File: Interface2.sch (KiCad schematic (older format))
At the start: 6 parts, among them U55 SN74LV165APWR, U56 SN74LV165APWR, U57 SN74LVC126APWR, U58 SN74LVC126APWR

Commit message: PVT
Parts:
- U52: renamed from U55; footprint IC-SOP:TSSOP16-W4.4_Hand -> IC-SOP:TSSOP16-W4.4
- U53: renamed from U56; footprint IC-SOP:TSSOP16-W4.4_Hand -> IC-SOP:TSSOP16-W4.4
- U54: renamed from U57; footprint IC-SOP:TSSOP14-W4.4_Hand -> IC-SOP:TSSOP14-W4.4
- U55: renamed from U58; footprint IC-SOP:TSSOP14-W4.4_Hand -> IC-SOP:TSSOP14-W4.4
- renumbered C238 to C229, C239 to C230
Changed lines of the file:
@@
 $Descr A4 11693 8268
 encoding utf-8
-Sheet 24 24
-Title "Phoenix DVT"
-Date "2020-05-18"
+Sheet 23 24
+Title "Phoenix PVT"
+Date "2020-07-19"
 Rev "1"
 Comp ""
@@
 $EndDescr
 $Comp
-L logic:74165 U56
+L logic:74165 U53
 U 1 1 5E4719EB
 P 2500 4600
-F 0 "U56" H 2500 5350 50  0000 C CNN
+F 0 "U53" H 2500 5350 50  0000 C CNN
 F 1 "SN74LV165APWR" H 2500 3850 50  0000 C CNN
-F 2 "IC-SOP:TSSOP16-W4.4_Hand" H 2500 4600 50  0001 C CNN
+F 2 "IC-SOP:TSSOP16-W4.4" H 2500 4600 50  0001 C CNN
 F 3 "" H 2500 4600 50  0001 C CNN
 F 4 "SN74LV165APWR" H 2500 4600 50  0001 C CNN "PartName"
@@
 P 2000 4400
 AR Path="/5E47EDCF" Ref="#PWR?"  Part="1"
-AR Path="/5F235278/5E47EDCF" Ref="#PWR0446"  Part="1"
-F 0 "#PWR0446" H 2000 4150 50  0001 C CNN
+AR Path="/5F235278/5E47EDCF" Ref="#PWR0426"  Part="1"
+F 0 "#PWR0426" H 2000 4150 50  0001 C CNN
 F 1 "GND" H 2000 4250 50  0000 C CNN
 F 2 "" H 2000 4400 50  0001 C CNN
@@
 P 2000 5200
 AR Path="/5E47F172" Ref="#PWR?"  Part="1"
-AR Path="/5F235278/5E47F172" Ref="#PWR0447"  Part="1"
-F 0 "#PWR0447" H 2000 4950 50  0001 C CNN
+AR Path="/5F235278/5E47F172" Ref="#PWR0427"  Part="1"
+F 0 "#PWR0427" H 2000 4950 50  0001 C CNN
 F 1 "GND" H 2000 5050 50  0000 C CNN
 F 2 "" H 2000 5200 50  0001 C CNN
@@
 	2000 4400 2100 4400
 $Comp
-L supply-value:+3V3 #PWR0445
+L supply-value:+3V3 #PWR0425
 U 1 1 5E48BD16
 P 2000 4000
-F 0 "#PWR0445" H 2000 3850 50  0001 C CNN
+F 0 "#PWR0425" H 2000 3850 50  0001 C CNN
 F 1 "+3V3" H 2000 4140 50  0000 C CNN
 F 2 "" H 2000 4000 50  0001 C CNN
@@
 	2900 5100 3300 5100
 $Comp
-L logic:74165 U55
+L logic:74165 U52
 U 1 1 5E6F7AF5
 P 2500 1600
-F 0 "U55" H 2500 2350 50  0000 C CNN
+F 0 "U52" H 2500 2350 50  0000 C CNN
 F 1 "SN74LV165APWR" H 2500 850 50  0000 C CNN
-F 2 "IC-SOP:TSSOP16-W4.4_Hand" H 2500 1600 50  0001 C CNN
+F 2 "IC-SOP:TSSOP16-W4.4" H 2500 1600 50  0001 C CNN
 F 3 "" H 2500 1600 50  0001 C CNN
 F 4 "SN74LV165APWR" H 2500 1600 50  0001 C CNN "PartName"
@@
 P 2000 1400
 AR Path="/5E6F7AFF" Ref="#PWR?"  Part="1"
-AR Path="/5F235278/5E6F7AFF" Ref="#PWR0443"  Part="1"
-F 0 "#PWR0443" H 2000 1150 50  0001 C CNN
+AR Path="/5F235278/5E6F7AFF" Ref="#PWR0423"  Part="1"
+F 0 "#PWR0423" H 2000 1150 50  0001 C CNN
 F 1 "GND" H 2000 1250 50  0000 C CNN
 F 2 "" H 2000 1400 50  0001 C CNN
@@
 P 2000 2200
 AR Path="/5E6F7B05" Ref="#PWR?"  Part="1"
-AR Path="/5F235278/5E6F7B05" Ref="#PWR0444"  Part="1"
-F 0 "#PWR0444" H 2000 1950 50  0001 C CNN
+AR Path="/5F235278/5E6F7B05" Ref="#PWR0424"  Part="1"
+F 0 "#PWR0424" H 2000 1950 50  0001 C CNN
 F 1 "GND" H 2000 2050 50  0000 C CNN
 F 2 "" H 2000 2200 50  0001 C CNN
@@
 	2000 1400 2100 1400
 $Comp
-L supply-value:+3V3 #PWR0442
+L supply-value:+3V3 #PWR0422
 U 1 1 5E6F7B0D
 P 2000 1000
-F 0 "#PWR0442" H 2000 850 50  0001 C CNN
+F 0 "#PWR0422" H 2000 850 50  0001 C CNN
 F 1 "+3V3" H 2000 1140 50  0000 C CNN
 F 2 "" H 2000 1000 50  0001 C CNN
@@
 	2000 1000 2100 1000
 $Comp
-L passive:C C238
+L passive:C C229
 U 1 1 5E6F7B22
 P 2000 1200
-F 0 "C238" H 2100 1250 50  0000 L CNN
+F 0 "C229" H 2100 1250 50  0000 L CNN
 F 1 "100n" H 2100 1150 50  0000 L CNN
 F 2 "Capacitor-Chip:C_CHIP_1005_Hand_NoSilk" H 2100 1100 50  0001 C CNN
@@
 P 7400 1200
 AR Path="/5E96614B" Ref="#PWR?"  Part="1"
-AR Path="/5F235278/5E96614B" Ref="#PWR0453"  Part="1"
-F 0 "#PWR0453" H 7400 950 50  0001 C CNN
+AR Path="/5F235278/5E96614B" Ref="#PWR0433"  Part="1"
+F 0 "#PWR0433" H 7400 950 50  0001 C CNN
 F 1 "GND" H 7400 1050 50  0000 C CNN
 F 2 "" H 7400 1200 50  0001 C CNN
@@
 	7400 1200 7600 1200
 $Comp
-L supply-value:+3V3 #PWR0451
+L supply-value:+3V3 #PWR0431
 U 1 1 5E966152
 P 7200 1000
-F 0 "#PWR0451" H 7200 850 50  0001 C CNN
+F 0 "#PWR0431" H 7200 850 50  0001 C CNN
 F 1 "+3V3" H 7200 1140 50  0000 C CNN
 F 2 "" H 7200 1000 50  0001 C CNN
@@
 	9000 2400 8400 2400
 $Comp
-L passive:C C239
+L passive:C C230
 U 1 1 5E499CE1
 P 2000 4200
-F 0 "C239" H 2100 4250 50  0000 L CNN
+F 0 "C230" H 2100 4250 50  0000 L CNN
 F 1 "100n" H 2100 4150 50  0000 L CNN
 F 2 "Capacitor-Chip:C_CHIP_1005_Hand_NoSilk" H 2100 4100 50  0001 C CNN
@@
 MOTOR4_ENC_B_5V
 $Comp
-L logic:74126 U57
+L logic:74126 U54
 U 1 1 5F57B566
 P 8000 1700
-F 0 "U57" H 8000 2550 50  0000 C CNN
+F 0 "U54" H 8000 2550 50  0000 C CNN
 F 1 "SN74LVC126APWR" H 8000 850 50  0000 C CNN
-F 2 "IC-SOP:TSSOP14-W4.4_Hand" H 8000 1700 50  0001 C CNN
+F 2 "IC-SOP:TSSOP14-W4.4" H 8000 1700 50  0001 C CNN
 F 3 "" H 8000 1700 50  0001 C CNN
 F 4 "SN74LVC126APWR" H 8000 1700 50  0001 C CNN "PartName"
@@
 P 7400 4200
 AR Path="/5F5943F4" Ref="#PWR?"  Part="1"
-AR Path="/5F235278/5F5943F4" Ref="#PWR0454"  Part="1"
-F 0 "#PWR0454" H 7400 3950 50  0001 C CNN
+AR Path="/5F235278/5F5943F4" Ref="#PWR0434"  Part="1"
+F 0 "#PWR0434" H 7400 3950 50  0001 C CNN
 F 1 "GND" H 7400 4050 50  0000 C CNN
 F 2 "" H 7400 4200 50  0001 C CNN
@@
 	7400 4200 7600 4200
 $Comp
-L supply-value:+3V3 #PWR0452
+L supply-value:+3V3 #PWR0432
 U 1 1 5F5943FB
 P 7200 4000
-F 0 "#PWR0452" H 7200 3850 50  0001 C CNN
+F 0 "#PWR0432" H 7200 3850 50  0001 C CNN
 F 1 "+3V3" H 7200 4140 50  0000 C CNN
 F 2 "" H 7200 4000 50  0001 C CNN
@@
 Connection ~ 7200 5000
 $Comp
-L logic:74126 U58
+L logic:74126 U55
 U 1 1 5F594427
 P 8000 4700
-F 0 "U58" H 8000 5550 50  0000 C CNN
+F 0 "U55" H 8000 5550 50  0000 C CNN
 F 1 "SN74LVC126APWR" H 8000 3850 50  0000 C CNN
-F 2 "IC-SOP:TSSOP14-W4.4_Hand" H 8000 4700 50  0001 C CNN
+F 2 "IC-SOP:TSSOP14-W4.4" H 8000 4700 50  0001 C CNN
 F 3 "" H 8000 4700 50  0001 C CNN
 F 4 "SN74LVC126APWR" H 8000 4700 50  0001 C CNN "PartName"
@@
 P 3100 2300
 AR Path="/5E845F2B" Ref="#PWR?"  Part="1"
-AR Path="/5F235278/5E845F2B" Ref="#PWR0448"  Part="1"
-F 0 "#PWR0448" H 3100 2050 50  0001 C CNN
+AR Path="/5F235278/5E845F2B" Ref="#PWR0428"  Part="1"
+F 0 "#PWR0428" H 3100 2050 50  0001 C CNN
 F 1 "GND" H 3100 2150 50  0000 C CNN
 F 2 "" H 3100 2300 50  0001 C CNN
@@
 	3300 4900 2900 4900
 $Comp
-L supply-value:+5V #PWR0449
+L supply-value:+5V #PWR0429
 U 1 1 5F18DCAB
 P 7000 1300
-F 0 "#PWR0449" H 7000 1150 50  0001 C CNN
+F 0 "#PWR0429" H 7000 1150 50  0001 C CNN
 F 1 "+5V" H 7000 1440 50  0000 C CNN
 F 2 "" H 7000 1300 50  0001 C CNN
@@
 	7000 1400 7000 1300
 $Comp
-L supply-value:+5V #PWR0450
+L supply-value:+5V #PWR0430
 U 1 1 5F194AC5
 P 7000 4300
-F 0 "#PWR0450" H 7000 4150 50  0001 C CNN
+F 0 "#PWR0430" H 7000 4150 50  0001 C CNN
 F 1 "+5V" H 7000 4440 50  0000 C CNN
 F 2 "" H 7000 4300 50  0001 C CNN

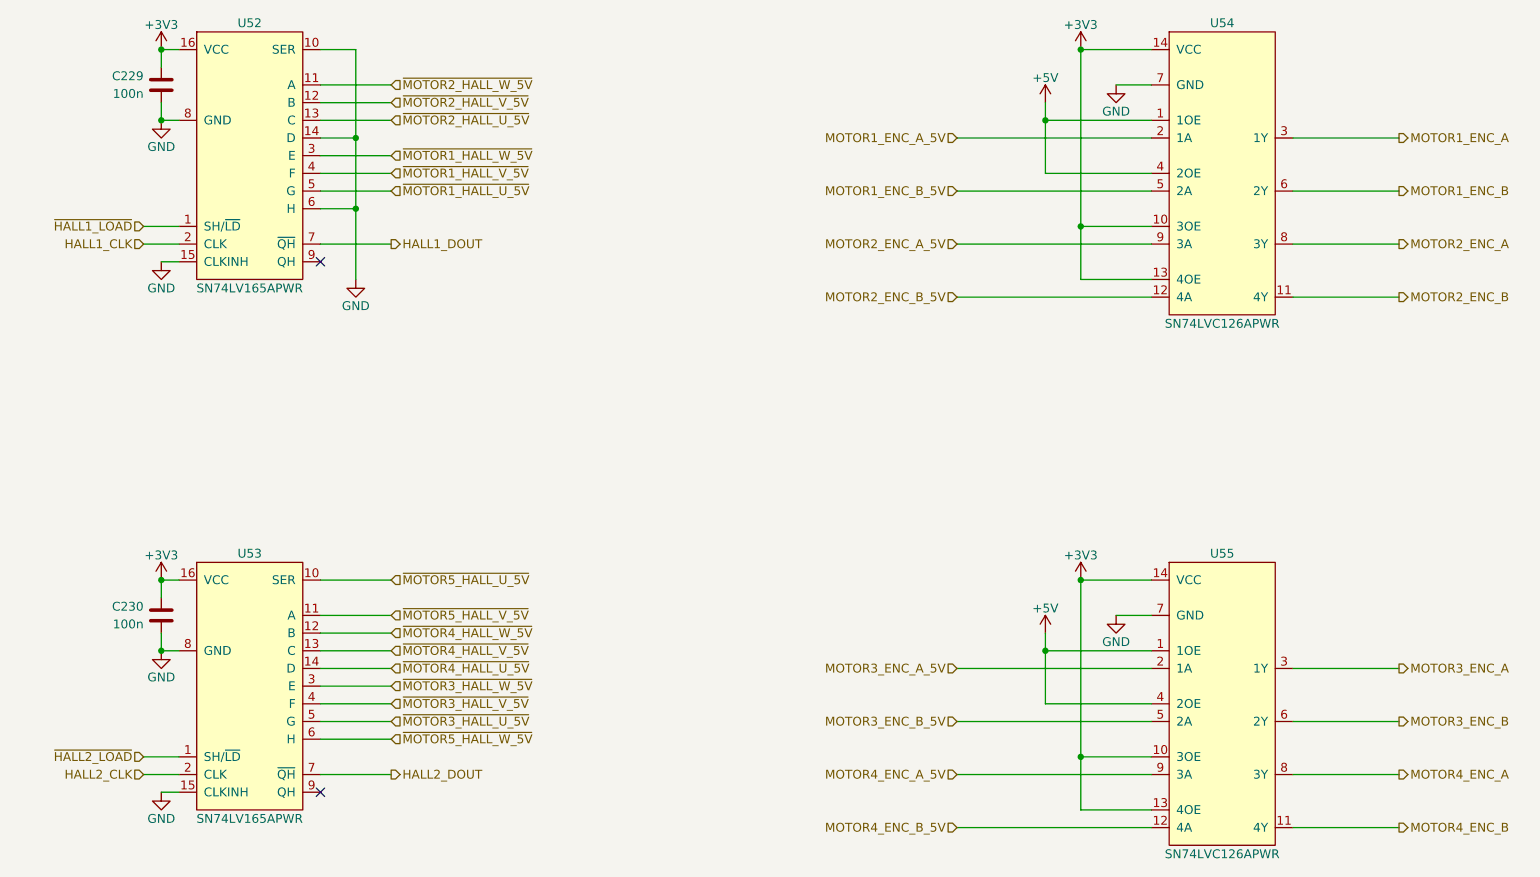
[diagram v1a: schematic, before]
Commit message: SBUにTVSダイオードを追加
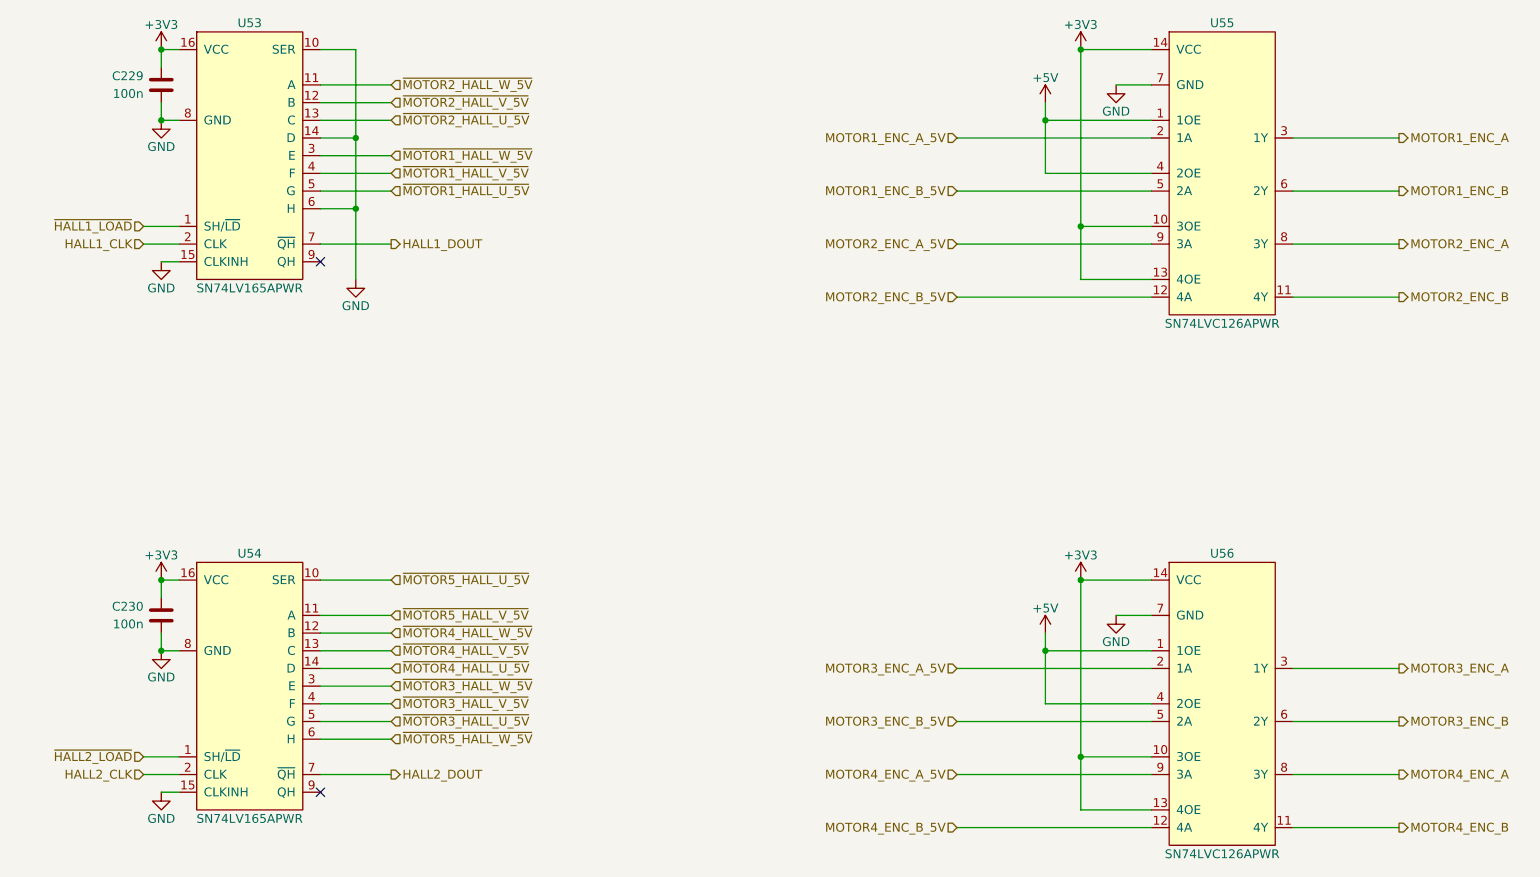
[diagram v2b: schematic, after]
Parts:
- renumbered U52 to U53, U53 to U54, U54 to U55, U55 to U56
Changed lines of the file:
@@
 $EndDescr
 $Comp
-L logic:74165 U53
+L logic:74165 U54
 U 1 1 5E4719EB
 P 2500 4600
-F 0 "U53" H 2500 5350 50  0000 C CNN
+F 0 "U54" H 2500 5350 50  0000 C CNN
 F 1 "SN74LV165APWR" H 2500 3850 50  0000 C CNN
 F 2 "IC-SOP:TSSOP16-W4.4" H 2500 4600 50  0001 C CNN
@@
 	2900 5100 3300 5100
 $Comp
-L logic:74165 U52
+L logic:74165 U53
 U 1 1 5E6F7AF5
 P 2500 1600
-F 0 "U52" H 2500 2350 50  0000 C CNN
+F 0 "U53" H 2500 2350 50  0000 C CNN
 F 1 "SN74LV165APWR" H 2500 850 50  0000 C CNN
 F 2 "IC-SOP:TSSOP16-W4.4" H 2500 1600 50  0001 C CNN
@@
 MOTOR4_ENC_B_5V
 $Comp
-L logic:74126 U54
+L logic:74126 U55
 U 1 1 5F57B566
 P 8000 1700
-F 0 "U54" H 8000 2550 50  0000 C CNN
+F 0 "U55" H 8000 2550 50  0000 C CNN
 F 1 "SN74LVC126APWR" H 8000 850 50  0000 C CNN
 F 2 "IC-SOP:TSSOP14-W4.4" H 8000 1700 50  0001 C CNN
@@
 Connection ~ 7200 5000
 $Comp
-L logic:74126 U55
+L logic:74126 U56
 U 1 1 5F594427
 P 8000 4700
-F 0 "U55" H 8000 5550 50  0000 C CNN
+F 0 "U56" H 8000 5550 50  0000 C CNN
 F 1 "SN74LVC126APWR" H 8000 3850 50  0000 C CNN
 F 2 "IC-SOP:TSSOP14-W4.4" H 8000 4700 50  0001 C CNN

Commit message: FPGA_INTをFPGA_MODEに変更
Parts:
- U53, U54: symbol logic:74165 -> logic:74x165_001
- U55, U56: symbol logic:74126 -> logic:74x126_001
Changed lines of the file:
@@
 $EndDescr
 $Comp
-L logic:74165 U54
+L logic:74x165_001 U54
 U 1 1 5E4719EB
 P 2500 4600
@@
 	2900 5100 3300 5100
 $Comp
-L logic:74165 U53
+L logic:74x165_001 U53
 U 1 1 5E6F7AF5
 P 2500 1600
@@
 MOTOR4_ENC_B_5V
 $Comp
-L logic:74126 U55
+L logic:74x126_001 U55
 U 1 1 5F57B566
 P 8000 1700
+AR Path="/5F57B566" Ref="U55"  Part="1"
+AR Path="/5F235278/5F57B566" Ref="U55"  Part="1"
 F 0 "U55" H 8000 2550 50  0000 C CNN
 F 1 "SN74LVC126APWR" H 8000 850 50  0000 C CNN
@@
 Connection ~ 7200 5000
 $Comp
-L logic:74126 U56
+L logic:74x126_001 U56
 U 1 1 5F594427
 P 8000 4700
+AR Path="/5F594427" Ref="U56"  Part="1"
+AR Path="/5F235278/5F594427" Ref="U56"  Part="1"
 F 0 "U56" H 8000 5550 50  0000 C CNN
 F 1 "SN74LVC126APWR" H 8000 3850 50  0000 C CNN
